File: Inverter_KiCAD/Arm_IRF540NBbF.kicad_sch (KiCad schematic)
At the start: 23 parts, among them Q1 IRF540N, Q2 IRF540N, Q7 HCPL-315J-500E, U1 GO 10-SME/SP3, U12 HCPL-7800A

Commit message: assigments footprints
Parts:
- removed U5 (x2): ~, symbol MPRB2415S-6W:MPRB2415S-6W
- added U1, U18: MPRB2415S-6W, Custom:MPRB2415S, symbol MPRB2415S-6W:MPRB2415S-6W
- C1: renamed from C10; footprint (none) -> Capacitor_SMD:CP_Elec_6.3x7.7; MFR (none) -> 865060445005
- C10: renamed from C7; footprint (none) -> Capacitor_SMD:C_0603_1608Metric_Pad1.08x0.95mm_HandSolder
- C2: renamed from C16; footprint (none) -> Capacitor_SMD:CP_Elec_6.3x7.7; MFR (none) -> 865060445005
- C3: renamed from C13; footprint (none) -> Capacitor_SMD:CP_Elec_5x5.4; MFR (none) -> 865060442002
- C4: renamed from C19; footprint (none) -> Capacitor_SMD:CP_Elec_5x5.4; MFR (none) -> 865060442002
- C5: renamed from C24; footprint (none) -> Capacitor_SMD:C_0603_1608Metric_Pad1.08x0.95mm_HandSolder
- C6: renamed from C30; footprint (none) -> Capacitor_SMD:C_0603_1608Metric_Pad1.08x0.95mm_HandSolder
- C7: renamed from C27; footprint (none) -> Capacitor_SMD:C_0603_1608Metric_Pad1.08x0.95mm_HandSolder
- C8: renamed from C1; footprint (none) -> Capacitor_SMD:C_0603_1608Metric_Pad1.08x0.95mm_HandSolder
- C9: renamed from C4; footprint (none) -> Capacitor_SMD:C_0603_1608Metric_Pad1.08x0.95mm_HandSolder
- Q1: renamed from Q7; footprint SO-16_HCPL-315J_BRA -> Custom:SO-16_HCPL-315J_BRA
- R1: footprint (none) -> Resistor_SMD:R_0603_1608Metric_Pad0.98x0.95mm_HandSolder
- R2: renamed from R4; footprint (none) -> Resistor_SMD:R_0603_1608Metric_Pad0.98x0.95mm_HandSolder
- R3: renamed from R7; footprint (none) -> Resistor_SMD:R_0603_1608Metric_Pad0.98x0.95mm_HandSolder
- R4: renamed from R10; footprint (none) -> Resistor_SMD:R_0603_1608Metric_Pad0.98x0.95mm_HandSolder
- R5: renamed from R13; footprint (none) -> Resistor_SMD:R_0603_1608Metric_Pad0.98x0.95mm_HandSolder
- R6: renamed from R16; footprint (none) -> Resistor_SMD:R_0603_1608Metric_Pad0.98x0.95mm_HandSolder
- U3: renamed from U12; footprint 300mil_DIP-8_BRA -> HCPL-7800A:HCPL-7800A
- U4: renamed from U1; footprint SOIC8-GO-SME/SP3_LEM -> GO-10-SME:SOIC8-GO-SME&slash_SP3_LEM
- renumbered Q1 to Q2, Q2 to Q3
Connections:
- net ARM_OUT: now also U18.7 (0V)
- net GND: now also U1.7 (0V)
- net ISO_15V: now also U1.2 (Vin), U18.2 (Vin)
- net ISO_GND: now also U1.1 (GND), U18.1 (GND)
- net PwrEn: now also U1.3 (Ctrl), U18.3 (Ctrl)
- net VCC_H: now also U18.6 (Vout)
- net VCC_L: now also U1.6 (Vout)

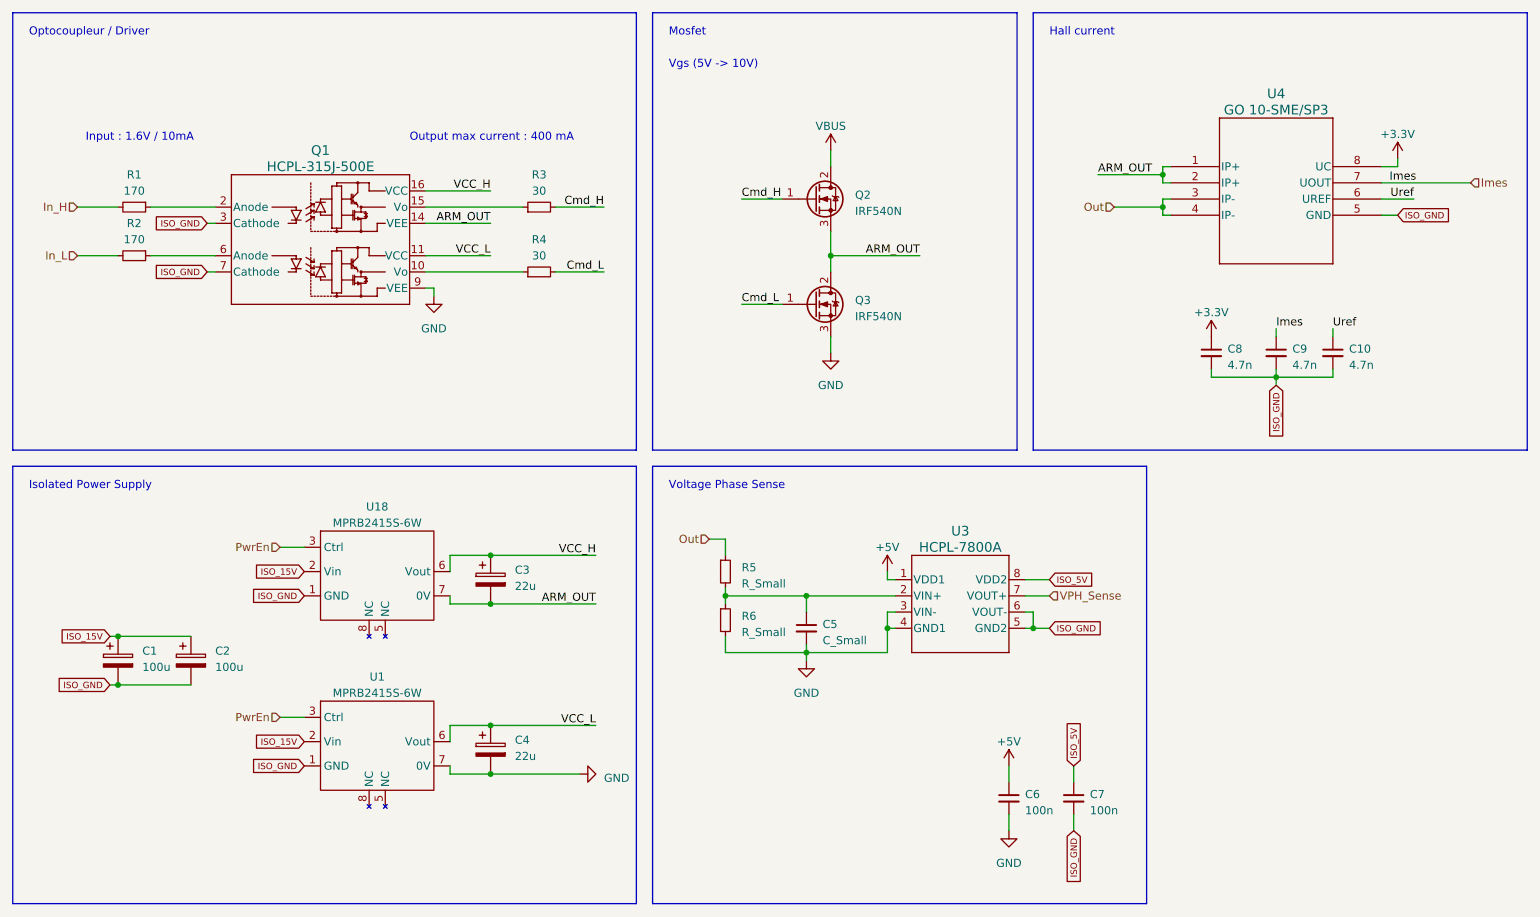
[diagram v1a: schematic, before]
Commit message: update schematic
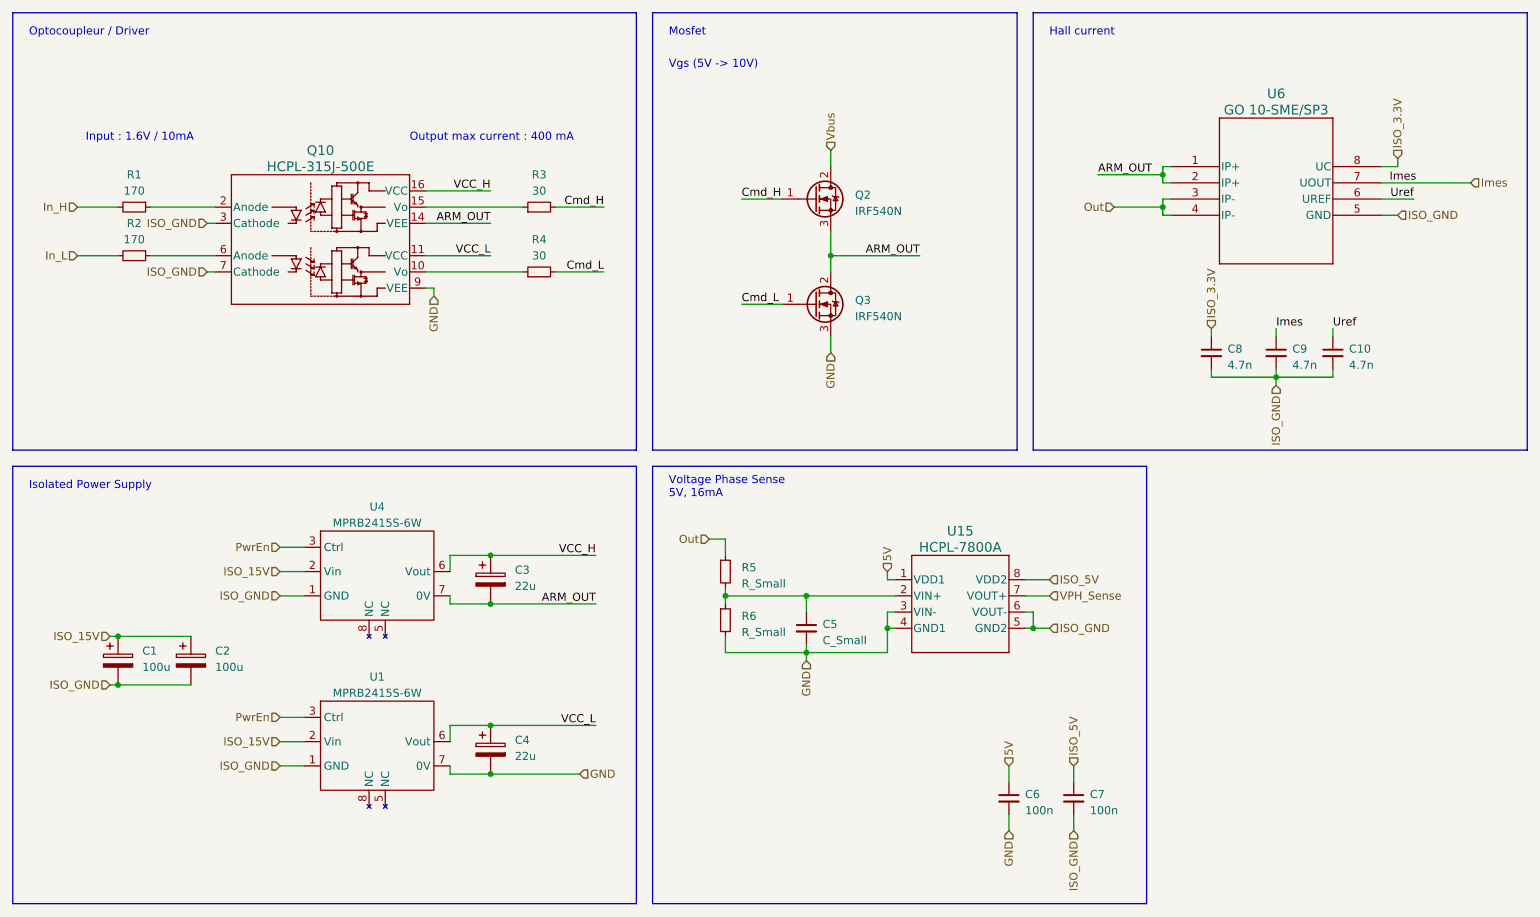
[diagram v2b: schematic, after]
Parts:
- removed Q1: HCPL-315J-500E, Custom:SO-16_HCPL-315J_BRA, symbol HCPL-315J-500E:HCPL-315J-500E
- removed U1, U18: MPRB2415S-6W, Custom:MPRB2415S, symbol MPRB2415S-6W:MPRB2415S-6W
- removed U3: HCPL-7800A, HCPL-7800A:HCPL-7800A, symbol HCPL-7800A:HCPL-7800A
- removed U4: GO 10-SME/SP3, GO-10-SME:SOIC8-GO-SME&slash_SP3_LEM, symbol GO-10-SME:GO_10-SME
- added Q10: HCPL-315J-500E, Custom:SO-16_HCPL-315J_BRA, symbol Custom:HCPL-315J-500E
- added U1, U4: MPRB2415S-6W, Custom:MPRB2415S, symbol Custom:MPRB2415S-6W
- added U15: HCPL-7800A, Custom:HCPL-7800A, symbol Custom:HCPL-7800A
- added U6: GO 10-SME/SP3, Custom:SOIC8-GO-SME&slash_SP3_LEM, symbol Custom:GO_10-SME
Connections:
- net ARM_OUT: now also Q10.14 (VEE), U4.7 (0V), U6.1 (IP+), U6.2 (IP+)
- net GND: now also Q10.9 (VEE), U1.7 (0V), U15.3 (VIN-), U15.4 (GND1)
- net ISO_15V: now also U1.2 (Vin), U4.2 (Vin)
- net ISO_5V: now also U15.8 (VDD2)
- net ISO_GND: now also Q10.3 (Cathode), Q10.7 (Cathode), U1.1 (GND), U15.5 (GND2), U15.6 (VOUT-), U4.1 (GND), U6.5 (GND)
- net Imes: now also U6.7 (UOUT)
- net Out: now also U6.3 (IP-), U6.4 (IP-)
- net PwrEn: now also U1.3 (Ctrl), U4.3 (Ctrl)
- net Uref: now also U6.6 (UREF)
- net VCC_H: now also Q10.16 (VCC), U4.6 (Vout)
- net VCC_L: now also Q10.11 (VCC), U1.6 (Vout)
- net VPH_Sense: now also U15.7 (VOUT+)
- net at R1.1: now also Q10.2 (Anode)
- net at R3.1: now also Q10.15 (Vo)
- net at C5.1, R5.2, R6.1: now also U15.2 (VIN+)
- net at R2.1: now also Q10.6 (Anode)
- net at R4.1: now also Q10.10 (Vo)
- net +3.3V renamed ISO_3.3V
- net ISO_3.3V: now also U6.8 (UC)
- net +5V renamed 5V
- net 5V: now also U15.1 (VDD1)
- net VBUS renamed Vbus
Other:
- note added: "Voltage Phase Sense 5V, 16mA"
- note removed: "Voltage Phase Sense"

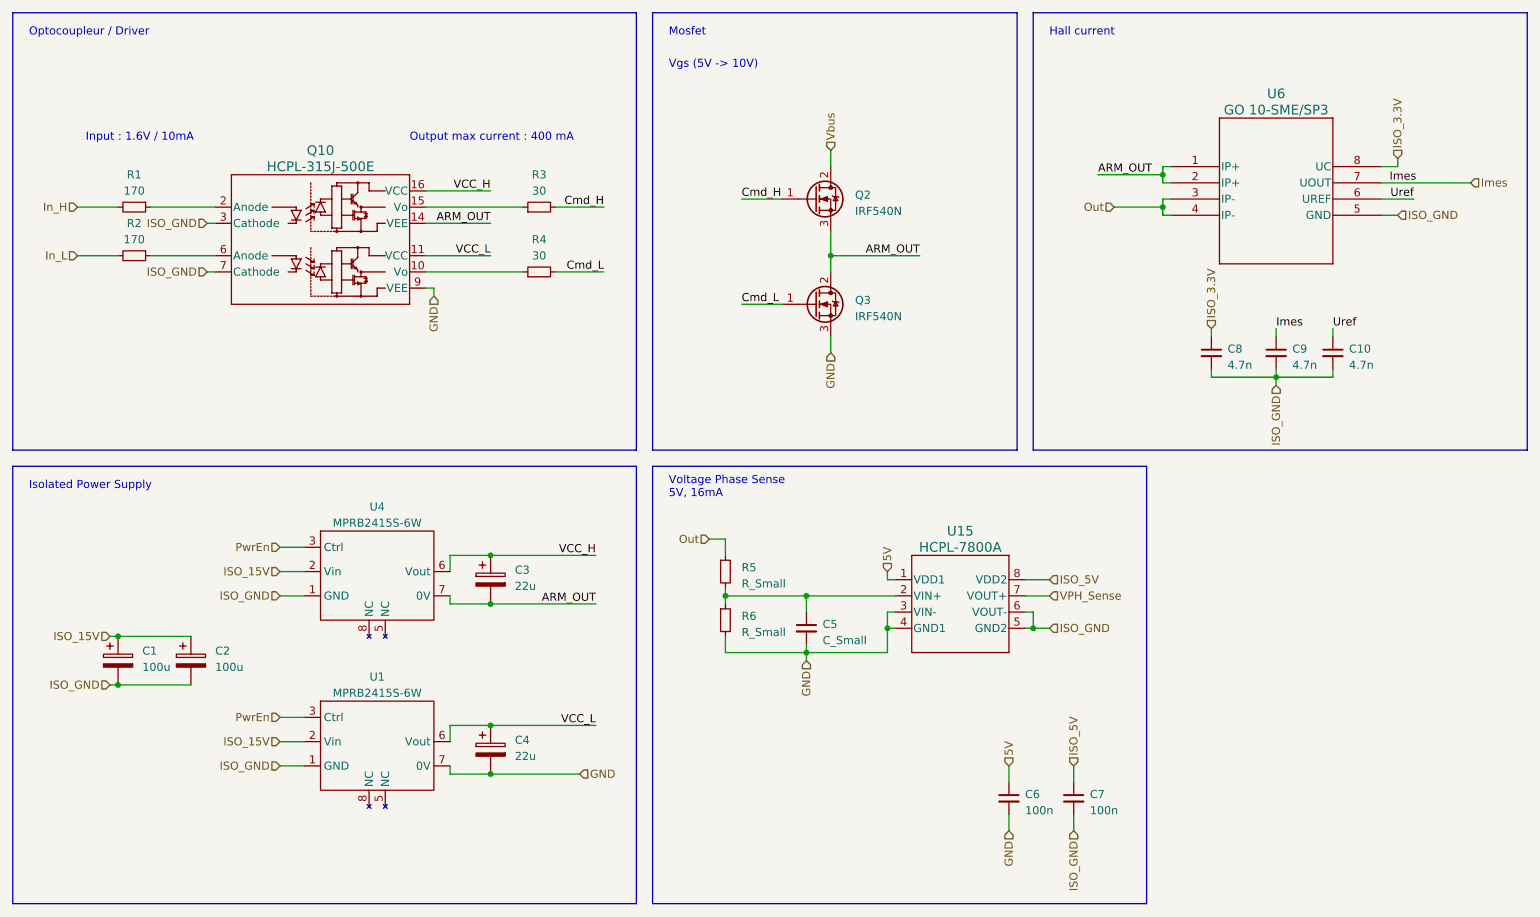
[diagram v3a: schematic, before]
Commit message: update schematic
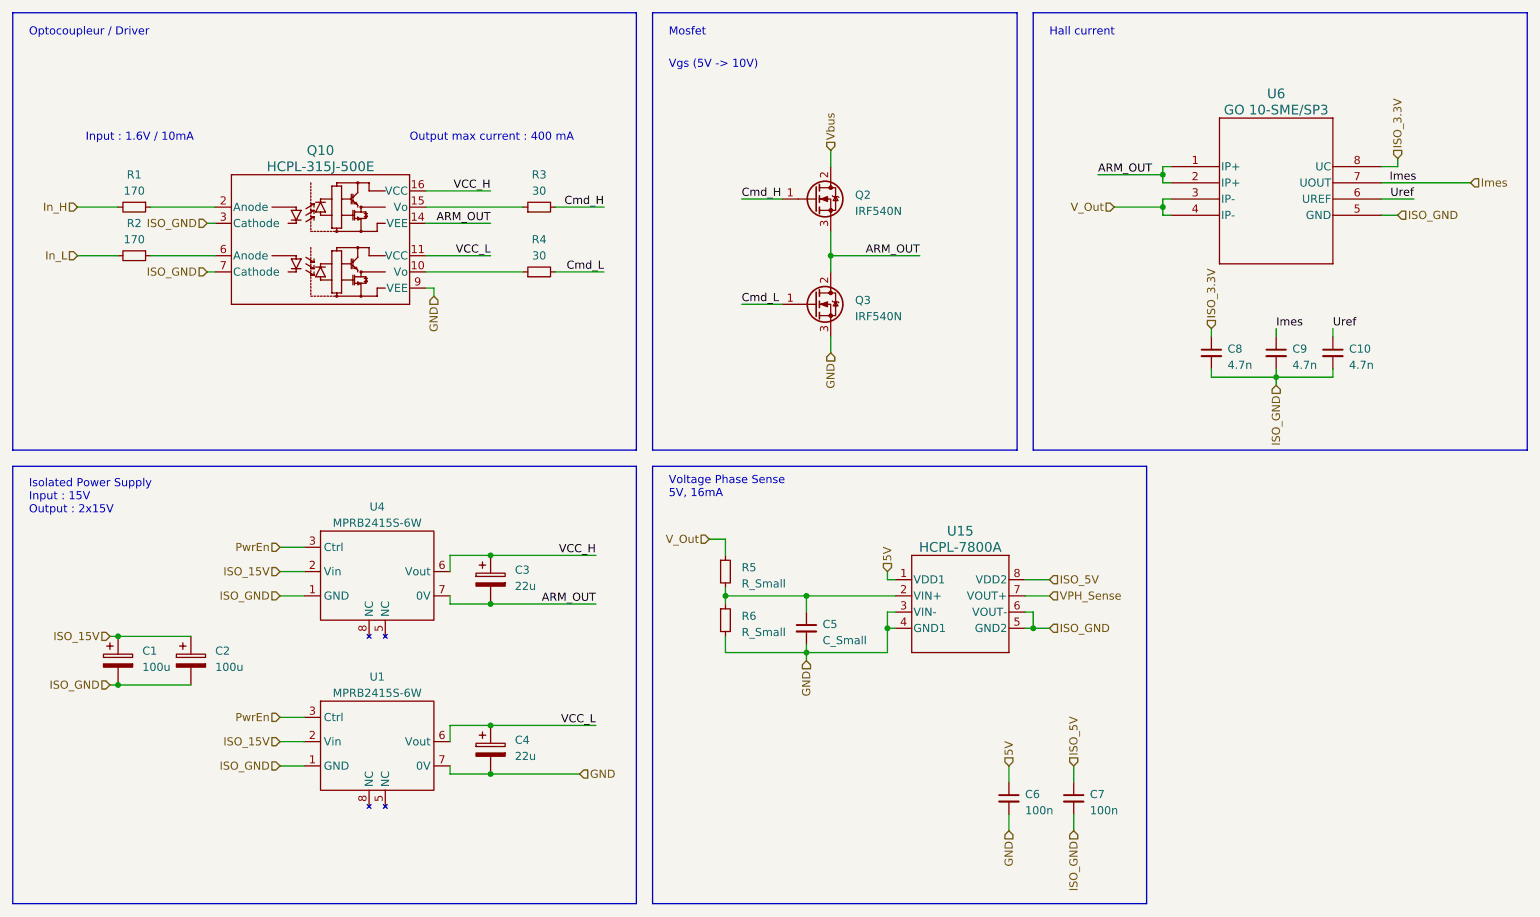
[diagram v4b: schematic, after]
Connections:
- net Out renamed V_Out
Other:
- note added: "Isolated Power Supply Input : 15V Output : 2x15V"
- note removed: "Isolated Power Supply"
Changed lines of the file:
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@@
     (effects (font (size 1.27 1.27)) (justify left bottom))
   )
-  (text "Isolated Power Supply" (at 16.51 88.9 0)
+  (text "Isolated Power Supply\nInput : 15V\nOutput : 2x15V" (at 16.51 92.71 0)
     (effects (font (size 1.27 1.27)) (justify left bottom))
   )
@@
     (effects (font (size 1.27 1.27)) (justify left bottom))
   )
-  (hierarchical_label "Out" (shape input) (at 123.19 96.52 180) (fields_autoplaced)
+  (hierarchical_label "V_Out" (shape input) (at 123.19 96.52 180) (fields_autoplaced)
     (effects (font (size 1.27 1.27)) (justify right))
   )
@@
     (effects (font (size 1.27 1.27)) (justify left))
   )
+  (hierarchical_label "V_Out" (shape input) (at 186.69 44.45 180) (fields_autoplaced)
+    (effects (font (size 1.27 1.27)) (justify right))
+  )
   (hierarchical_label "5V" (shape input) (at 170.18 132.08 90) (fields_autoplaced)
     (effects (font (size 1.27 1.27)) (justify left))
@@
     (effects (font (size 1.27 1.27)) (justify right))
   )
-  (hierarchical_label "Out" (shape input) (at 186.69 44.45 180) (fields_autoplaced)
-    (effects (font (size 1.27 1.27)) (justify right))
-  )

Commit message: add break
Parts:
- C10, C6, C7, C8, C9: footprint Capacitor_SMD:C_0603_1608Metric_Pad1.08x0.95mm_HandSolder -> Capacitor_SMD:C_0402_1005Metric_Pad0.74x0.62mm_HandSolder
- R3, R4: footprint Resistor_SMD:R_0603_1608Metric_Pad0.98x0.95mm_HandSolder -> Resistor_SMD:R_1206_3216Metric_Pad1.30x1.75mm_HandSolder
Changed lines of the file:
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@@
       (effects (font (size 1.27 1.27)) (justify left))
     )
-    (property "Footprint" "Capacitor_SMD:C_0603_1608Metric_Pad1.08x0.95mm_HandSolder" (at 220.98 67.31 0)
+    (property "Footprint" "Capacitor_SMD:C_0402_1005Metric_Pad0.74x0.62mm_HandSolder" (at 220.98 67.31 0)
       (effects (font (size 1.27 1.27)) hide)
     )
@@
       (effects (font (size 1.27 1.27)) (justify left))
     )
-    (property "Footprint" "Capacitor_SMD:C_0603_1608Metric_Pad1.08x0.95mm_HandSolder" (at 170.18 137.16 0)
+    (property "Footprint" "Capacitor_SMD:C_0402_1005Metric_Pad0.74x0.62mm_HandSolder" (at 170.18 137.16 0)
       (effects (font (size 1.27 1.27)) hide)
     )
@@
       (effects (font (size 1.27 1.27)))
     )
-    (property "Footprint" "Resistor_SMD:R_0603_1608Metric_Pad0.98x0.95mm_HandSolder" (at 96.52 44.45 0)
+    (property "Footprint" "Resistor_SMD:R_1206_3216Metric_Pad1.30x1.75mm_HandSolder" (at 96.52 44.45 0)
       (effects (font (size 1.27 1.27)) hide)
     )
@@
       (effects (font (size 1.27 1.27)) (justify left))
     )
-    (property "Footprint" "Capacitor_SMD:C_0603_1608Metric_Pad1.08x0.95mm_HandSolder" (at 212.09 67.31 0)
+    (property "Footprint" "Capacitor_SMD:C_0402_1005Metric_Pad0.74x0.62mm_HandSolder" (at 212.09 67.31 0)
       (effects (font (size 1.27 1.27)) hide)
     )
@@
       (effects (font (size 1.27 1.27)))
     )
-    (property "Footprint" "Resistor_SMD:R_0603_1608Metric_Pad0.98x0.95mm_HandSolder" (at 96.52 54.61 0)
+    (property "Footprint" "Resistor_SMD:R_1206_3216Metric_Pad1.30x1.75mm_HandSolder" (at 96.52 54.61 0)
       (effects (font (size 1.27 1.27)) hide)
     )
@@
       (effects (font (size 1.27 1.27)) (justify left))
     )
-    (property "Footprint" "Capacitor_SMD:C_0603_1608Metric_Pad1.08x0.95mm_HandSolder" (at 201.93 67.31 0)
+    (property "Footprint" "Capacitor_SMD:C_0402_1005Metric_Pad0.74x0.62mm_HandSolder" (at 201.93 67.31 0)
       (effects (font (size 1.27 1.27)) hide)
     )
@@
       (effects (font (size 1.27 1.27)) (justify left))
     )
-    (property "Footprint" "Capacitor_SMD:C_0603_1608Metric_Pad1.08x0.95mm_HandSolder" (at 180.34 137.16 0)
-      (effects (font (size 1.27 1.27)) hide)
-    )
+    (property "Footprint" "Capacitor_SMD:C_0402_1005Metric_Pad0.74x0.62mm_HandSolder" (at 180.34 137.16 0)
+      (effects (font (size 1.27 1.27)) hide)
+    )
